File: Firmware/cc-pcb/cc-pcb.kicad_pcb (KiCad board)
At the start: 2 copper layers, 17 parts, among them CON1 BARREL_JACK, IC1 ATMEGA328P-A, P1 CONN_6, P2 CONN_6, P3 CONN_10, P4 CONN_6, P5 CONN_6, SW1 SRS

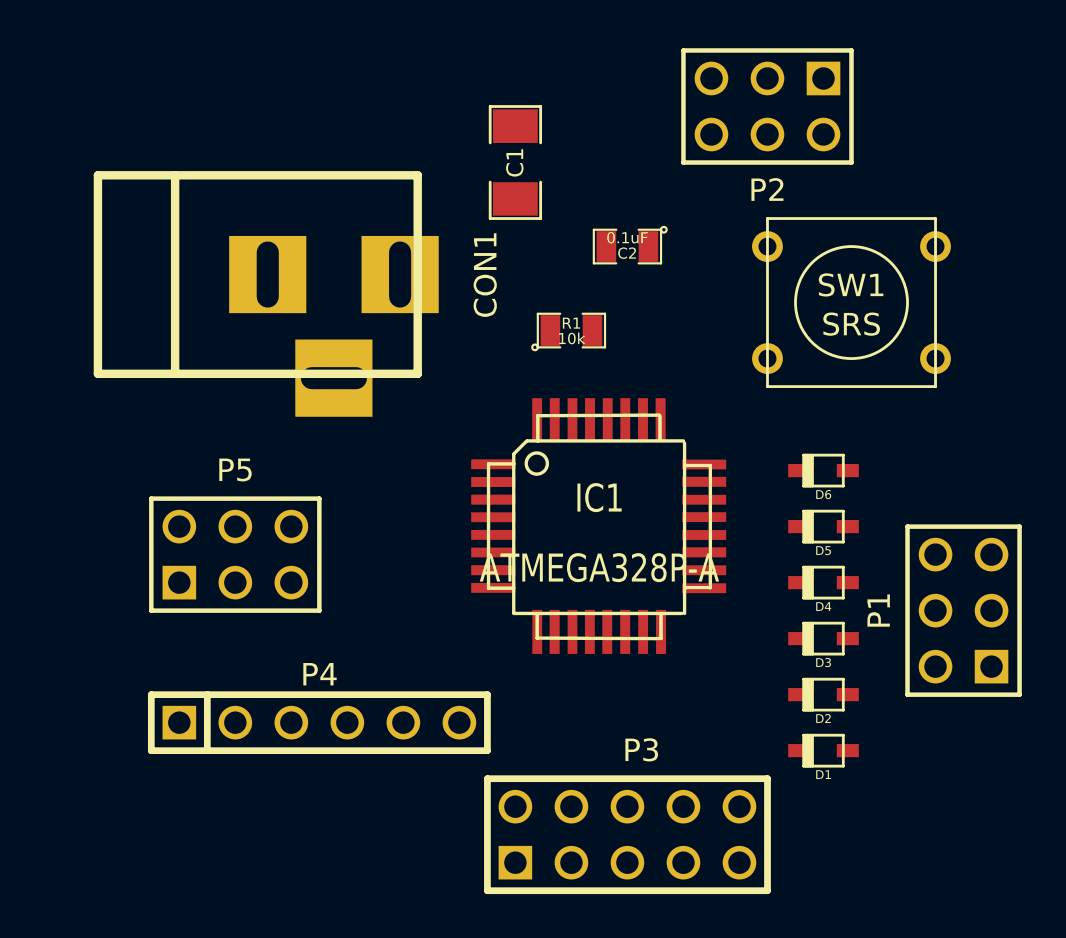
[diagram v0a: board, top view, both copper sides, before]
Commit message: Working on PCB, starting to make routes
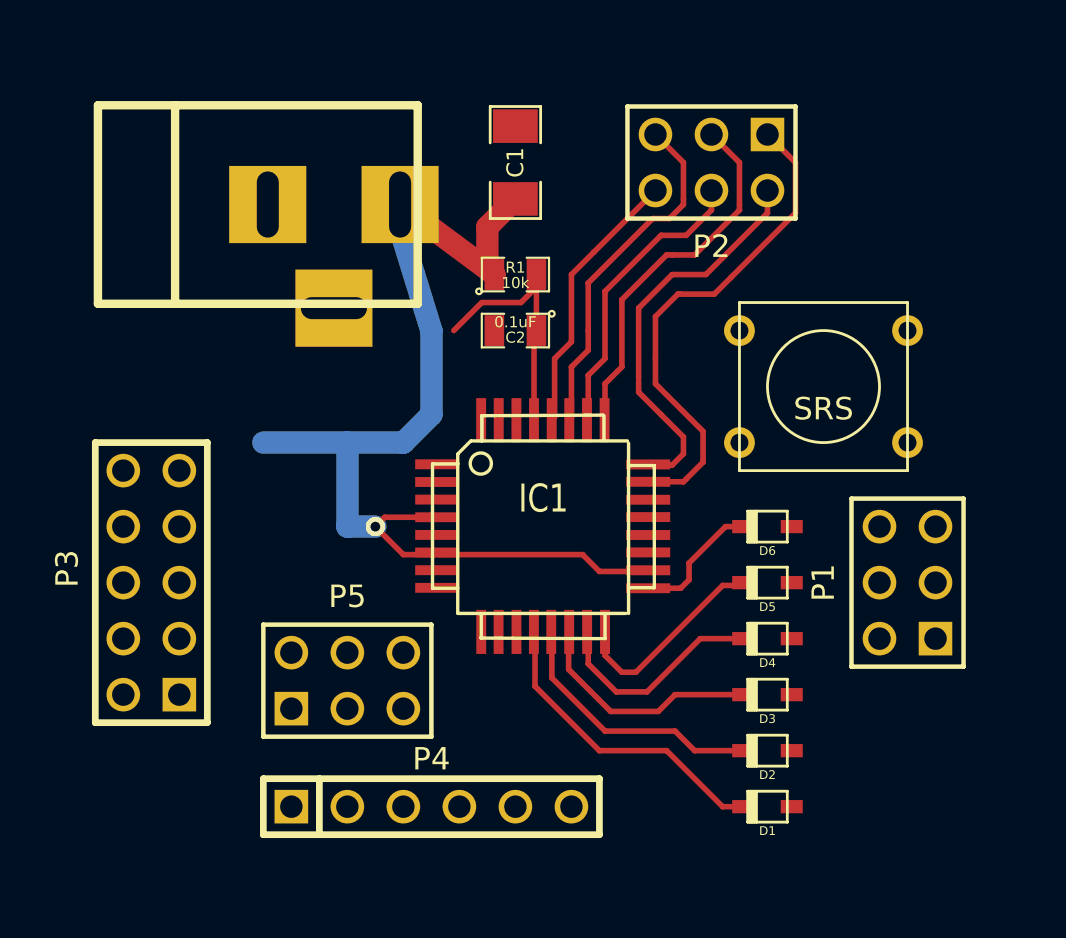
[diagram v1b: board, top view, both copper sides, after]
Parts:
- ?: renamed from CON1; value BARREL_JACK -> (none)
- IC1: value ATMEGA328P-A -> (none)
- P1, P2, P4, P5: value CONN_6 -> (none)
- P3: value CONN_10 -> (none)
- moved P3 24.4 mm to (153.7, 95.2), turned to 90 degrees
- moved P5 7.65 mm to (162.6, 99.7)
- moved P4 6.35 mm to (166.4, 105.4)
- moved C2 6.35 mm to (170.2, 83.8)
- moved ? 4.02 mm to (184.2, 86.4)
- moved P2 3.59 mm to (179.1, 76.2)
- moved D2 3.59 mm to (181.6, 102.9)
- moved D4 3.59 mm to (181.6, 97.8)
- moved D5 3.59 mm to (181.6, 95.2)
- moved D1 3.59 mm to (181.6, 105.4)
- moved D3 3.59 mm to (181.6, 100.3)
- moved D6 3.59 mm to (181.6, 92.7)
- moved R1 3.59 mm to (170.2, 81.3)
- moved ? 3.17 mm to (158.8, 78.1)
- moved P1 2.84 mm to (188.0, 95.2)
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- renumbered SW1 to ?
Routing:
- net VCC: track 0.00 -> 48.7 mm, vias 0 -> 1
- net N-000008: track 0.00 -> 22.7 mm
- net N-0000024: track 0.00 -> 17.8 mm
- net N-0000023: track 0.00 -> 16.8 mm
- net N-0000021: track 0.00 -> 16.1 mm
- net N-0000019: track 0.00 -> 14.3 mm
- net N-0000022: track 0.00 -> 13.4 mm
- net N-0000020: track 0.00 -> 12.4 mm
- net N-000009: track 0.00 -> 12.2 mm
- net N-0000029: track 0.00 -> 11.8 mm
- net N-0000018: track 0.00 -> 10.8 mm
- net N-0000017: track 0.00 -> 10.1 mm
- net N-0000016: track 0.00 -> 9.33 mm
- net N-0000015: track 0.00 -> 5.91 mm
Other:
- net class PWR added: clearance 0.508, trace_width 1.016, via_dia 0.889, via_drill 0.635

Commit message: Removed all traces from PCB
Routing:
- net VCC: track 48.7 -> 0.00 mm, vias 1 -> 0
- net N-000008: track 22.7 -> 0.00 mm
- net N-0000024: track 17.8 -> 0.00 mm
- net N-0000023: track 16.8 -> 0.00 mm
- net N-0000021: track 16.1 -> 0.00 mm
- net N-0000019: track 14.3 -> 0.14 mm
- net N-0000022: track 13.4 -> 0.00 mm
- net N-0000020: track 12.4 -> 0.00 mm
- net N-000009: track 12.2 -> 0.07 mm
- net N-0000029: track 11.8 -> 0.00 mm
- net N-0000018: track 10.8 -> 0.11 mm
- net N-0000017: track 10.1 -> 0.14 mm
- net N-0000016: track 9.33 -> 0.00 mm
- net N-0000015: track 5.91 -> 0.00 mm

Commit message: Working on PCB
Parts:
- moved P4 16.5 mm to (182.9, 105.4)
- moved P2 12.6 mm to (188.0, 85.1), turned to 90 degrees
- moved ? 10.9 mm to (177.8, 77.5)
- moved P5 6.75 mm to (167.6, 104.1)
- moved D2 6.48 mm to (180.3, 96.5)
- moved D4 6.48 mm to (180.3, 91.4)
- moved D1 6.48 mm to (180.3, 99.1)
- moved D3 6.48 mm to (180.3, 94.0)
- moved D5 6.48 mm to (180.3, 88.9)
- moved D6 6.48 mm to (180.3, 86.4)
- moved P3 5.24 mm to (158.8, 94.0)
- moved IC1 1.27 mm to (170.2, 92.7)
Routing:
- net VCC: track 0.00 -> 13.6 mm
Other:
- board outline added: 39.4 x 36.8 mm
- net class PWRIC added: clearance 0.254, trace_width 0.508, via_dia 0.889, via_drill 0.635
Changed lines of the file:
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@@
   (general
     (links 56)
-    (no_connects 56)
-    (area 148.7424 70.98792 192.8876 108.6866)
+    (no_connects 55)
+    (area 150.550879 70.98792 193.090001 109.270001)
     (thickness 1.6)
-    (drawings 0)
-    (tracks 11)
+    (drawings 4)
+    (tracks 14)
     (zones 0)
     (modules 17)
@@
     (add_net N-000008)
     (add_net N-000009)
-    (add_net VCC)
   )
   (net_class PWR ""
@@
     (uvia_drill 0.127)
   )
+  (net_class PWRIC ""
+    (clearance 0.254)
+    (trace_width 0.508)
+    (via_dia 0.889)
+    (via_drill 0.635)
+    (uvia_dia 0.508)
+    (uvia_drill 0.127)
+    (add_net VCC)
+  )
   (module TQFP32 (layer F.Cu)
-    (at 171.45 92.71)
+    (at 170.18 92.71)
     (fp_text reference IC1 (at 0 -1.27) (layer F.SilkS)
       (effects (font (size 1.27 1.016) (thickness 0.2032)))
@@
   )
   (module SW_PUSH_SMALL (layer F.Cu)
-    (at 184.15 86.36)
+    (at 177.8 77.47)
     (fp_text reference "" (at 0 -0.762) (layer F.SilkS)
       (effects (font (size 1.016 1.016) (thickness 0.2032)))
@@
   )
   (module sod323 (layer F.Cu)
-    (at 181.61 105.41 180)
+    (at 180.34 99.06 180)
     (descr SOD323)
     (fp_text reference D1 (at 0 -1.09982 180) (layer F.SilkS)
@@
   )
   (module sod323 (layer F.Cu)
-    (at 181.61 102.87 180)
+    (at 180.34 96.52 180)
     (descr SOD323)
     (fp_text reference D2 (at 0 -1.09982 180) (layer F.SilkS)
@@
   )
   (module sod323 (layer F.Cu)
-    (at 181.61 100.33 180)
+    (at 180.34 93.98 180)
     (descr SOD323)
     (fp_text reference D3 (at 0 -1.09982 180) (layer F.SilkS)
@@
   )
   (module sod323 (layer F.Cu)
-    (at 181.61 97.79 180)
+    (at 180.34 91.44 180)
     (descr SOD323)
     (fp_text reference D4 (at 0 -1.09982 180) (layer F.SilkS)
@@
   )
   (module sod323 (layer F.Cu)
-    (at 181.61 95.25 180)
+    (at 180.34 88.9 180)
     (descr SOD323)
     (fp_text reference D5 (at 0 -1.09982 180) (layer F.SilkS)
@@
   )
   (module sod323 (layer F.Cu)
-    (at 181.61 92.71 180)
+    (at 180.34 86.36 180)
     (descr SOD323)
     (fp_text reference D6 (at 0 -1.09982 180) (layer F.SilkS)
@@
   )
   (module PIN_ARRAY_5x2 (layer F.Cu)
-    (at 153.67 95.25 90)
+    (at 158.75 93.98 90)
     (descr "Double rangee de contacts 2 x 5 pins")
     (tags CONN)
@@
   )
   (module pin_array_3x2 (layer F.Cu)
-    (at 162.56 99.695)
+    (at 167.64 104.14)
     (descr "Double rangee de contacts 2 x 4 pins")
     (tags CONN)
@@
   )
   (module PIN_ARRAY-6X1 (layer F.Cu)
-    (at 166.37 105.41)
+    (at 182.88 105.41)
     (descr "Connecteur 6 pins")
     (tags "CONN DEV")
@@
   )
   (module pin_array_3x2 (layer F.Cu)
-    (at 179.07 76.2 180)
+    (at 187.96 85.09 90)
     (descr "Double rangee de contacts 2 x 4 pins")
     (tags CONN)
-    (fp_text reference P2 (at 0 -3.81 180) (layer F.SilkS)
-      (effects (font (size 1.016 1.016) (thickness 0.2032)))
-    )
-    (fp_text value "" (at 0 3.81 180) (layer F.SilkS) hide
+    (fp_text reference P2 (at 0 -3.81 90) (layer F.SilkS)
+      (effects (font (size 1.016 1.016) (thickness 0.2032)))
+    )
+    (fp_text value "" (at 0 3.81 90) (layer F.SilkS) hide
       (effects (font (size 1.016 1.016) (thickness 0.2032)))
     )
@@
     (fp_line (start 3.81 -2.54) (end 3.81 2.54) (layer F.SilkS) (width 0.2032))
     (fp_line (start -3.81 2.54) (end -3.81 -2.54) (layer F.SilkS) (width 0.2032))
-    (pad 1 thru_hole rect (at -2.54 1.27 180) (size 1.524 1.524) (drill 1.016)
+    (pad 1 thru_hole rect (at -2.54 1.27 90) (size 1.524 1.524) (drill 1.016)
       (layers *.Cu *.Mask F.SilkS)
       (net 29 N-000008)
     )
-    (pad 2 thru_hole circle (at -2.54 -1.27 180) (size 1.524 1.524) (drill 1.016)
+    (pad 2 thru_hole circle (at -2.54 -1.27 90) (size 1.524 1.524) (drill 1.016)
       (layers *.Cu *.Mask F.SilkS)
       (net 18 N-0000024)
     )
-    (pad 3 thru_hole circle (at 0 1.27 180) (size 1.524 1.524) (drill 1.016)
+    (pad 3 thru_hole circle (at 0 1.27 90) (size 1.524 1.524) (drill 1.016)
       (layers *.Cu *.Mask F.SilkS)
       (net 17 N-0000023)
     )
-    (pad 4 thru_hole circle (at 0 -1.27 180) (size 1.524 1.524) (drill 1.016)
+    (pad 4 thru_hole circle (at 0 -1.27 90) (size 1.524 1.524) (drill 1.016)
       (layers *.Cu *.Mask F.SilkS)
       (net 16 N-0000022)
     )
-    (pad 5 thru_hole circle (at 2.54 1.27 180) (size 1.524 1.524) (drill 1.016)
+    (pad 5 thru_hole circle (at 2.54 1.27 90) (size 1.524 1.524) (drill 1.016)
       (layers *.Cu *.Mask F.SilkS)
       (net 15 N-0000021)
     )
-    (pad 6 thru_hole circle (at 2.54 -1.27 180) (size 1.524 1.524) (drill 1.016)
+    (pad 6 thru_hole circle (at 2.54 -1.27 90) (size 1.524 1.524) (drill 1.016)
       (layers *.Cu *.Mask F.SilkS)
       (net 14 N-0000020)
@@
     )
   )
-  (segment (start 170.307 97.5614) (end 170.2308 97.4852) (width 0.254) (layer F.Cu) (net 2))
-  (segment (start 170.307 97.5614) (end 170.2308 97.4852) (width 0.254) (layer F.Cu) (net 2) (status 30))
-  (segment (start 173.482 97.536) (end 173.4312 97.4852) (width 0.254) (layer F.Cu) (net 10))
-  (segment (start 173.4312 97.4852) (end 173.482 97.536) (width 0.254) (layer F.Cu) (net 10) (status 30))
-  (segment (start 172.593 97.5106) (end 172.6184 97.4852) (width 0.254) (layer F.Cu) (net 11))
-  (segment (start 172.593 97.5106) (end 172.6184 97.4852) (width 0.254) (layer F.Cu) (net 11))
-  (segment (start 172.6184 97.4852) (end 172.593 97.5106) (width 0.254) (layer F.Cu) (net 11) (status 30))
-  (segment (start 171.069 97.536) (end 171.0182 97.4852) (width 0.254) (layer F.Cu) (net 12))
-  (segment (start 171.0182 97.4852) (end 171.069 97.536) (width 0.254) (layer F.Cu) (net 12) (status 30))
-  (segment (start 171.831 97.5106) (end 171.8056 97.4852) (width 0.254) (layer F.Cu) (net 30))
-  (segment (start 171.8056 97.4852) (end 171.831 97.5106) (width 0.254) (layer F.Cu) (net 30) (status 30))
+  (gr_line (start 153.67 109.22) (end 153.67 72.39) (angle 90) (layer Edge.Cuts) (width 0.1))
+  (gr_line (start 193.04 109.22) (end 153.67 109.22) (angle 90) (layer Edge.Cuts) (width 0.1))
+  (gr_line (start 193.04 72.39) (end 193.04 109.22) (angle 90) (layer Edge.Cuts) (width 0.1))
+  (gr_line (start 153.67 72.39) (end 193.04 72.39) (angle 90) (layer Edge.Cuts) (width 0.1))
+  (segment (start 169.037 97.5614) (end 168.9608 97.4852) (width 0.254) (layer F.Cu) (net 2) (status 30))
+  (segment (start 169.037 97.5614) (end 168.9608 97.4852) (width 0.254) (layer F.Cu) (net 2) (status 30))
+  (segment (start 172.212 97.536) (end 172.1612 97.4852) (width 0.254) (layer F.Cu) (net 10) (status 30))
+  (segment (start 172.1612 97.4852) (end 172.212 97.536) (width 0.254) (layer F.Cu) (net 10) (status 30))
+  (segment (start 171.323 97.5106) (end 171.3484 97.4852) (width 0.254) (layer F.Cu) (net 11) (status 30))
+  (segment (start 171.323 97.5106) (end 171.3484 97.4852) (width 0.254) (layer F.Cu) (net 11) (status 30))
+  (segment (start 171.3484 97.4852) (end 171.323 97.5106) (width 0.254) (layer F.Cu) (net 11) (status 30))
+  (segment (start 169.799 97.536) (end 169.7482 97.4852) (width 0.254) (layer F.Cu) (net 12) (status 30))
+  (segment (start 169.7482 97.4852) (end 169.799 97.536) (width 0.254) (layer F.Cu) (net 12) (status 30))
+  (segment (start 170.561 97.5106) (end 170.5356 97.4852) (width 0.254) (layer F.Cu) (net 30) (status 30))
+  (segment (start 170.5356 97.4852) (end 170.561 97.5106) (width 0.254) (layer F.Cu) (net 30) (status 30))
+  (segment (start 161.29 88.9) (end 160.02 88.9) (width 1.016) (layer B.Cu) (net 31))
+  (segment (start 164.95014 85.23986) (end 161.29 88.9) (width 1.016) (layer B.Cu) (net 31))
+  (segment (start 164.95014 78.105) (end 164.95014 85.23986) (width 1.016) (layer B.Cu) (net 31))
 )

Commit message: autorouter
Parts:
- moved D2 1.78 mm to (180.3, 98.3)
- moved D4 1.78 mm to (180.3, 93.2)
- moved D6 1.78 mm to (180.3, 88.1)
- moved D1 1.78 mm to (180.3, 100.8)
- moved D3 1.78 mm to (180.3, 95.8)
- moved D5 1.78 mm to (180.3, 90.7)
- turned P3 to 270 degrees
- gave numbers to parts that had none: 2
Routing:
- net GND: track 0.00 -> 111.3 mm, vias 0 -> 1
- net VCC: track 13.6 -> 85.5 mm, vias 0 -> 1
- net N-0000015: track 0.00 -> 56.4 mm
- net N-0000016: track 0.00 -> 56.3 mm, vias 0 -> 1
- net N-0000028: track 0.00 -> 53.5 mm
- net N-0000030: track 0.00 -> 51.6 mm
- net N-000007: track 0.00 -> 49.7 mm
- net N-0000029: track 0.00 -> 49.6 mm, vias 0 -> 1
- net N-0000032: track 0.00 -> 33.1 mm, vias 0 -> 1
- net N-0000017: track 0.14 -> 32.6 mm
- net N-0000021: track 0.00 -> 20.9 mm
- net N-0000020: track 0.00 -> 19.2 mm
- net N-0000023: track 0.00 -> 18.5 mm
- net N-000008: track 0.00 -> 17.8 mm
- net N-0000022: track 0.00 -> 16.5 mm
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
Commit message: added mounting holes
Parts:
- added 1PIN: P***, 1pin, F.Cu at (190.5, 106.7)
- added 1PIN: P***, 1pin, F.Cu at (190.5, 74.9)
- added 1PIN: P***, 1pin, F.Cu at (156.2, 106.7)
- moved P4 15.2 mm to (167.6, 105.4)
- moved P5 15.2 mm to (182.9, 104.1)
- moved D1 5.11 mm to (175.3, 100.3)
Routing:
- net N-0000015: track 56.4 -> 0.00 mm
- net N-0000016: track 56.3 -> 0.00 mm, vias 1 -> 0
- net N-0000028: track 53.5 -> 0.00 mm
- net N-0000030: track 51.6 -> 0.00 mm
- net N-0000029: track 49.6 -> 2.54 mm, vias 1 -> 0
- net N-000007: track 49.7 -> 9.88 mm
- net GND: track 111.3 -> 77.0 mm
- net N-0000017: track 32.6 -> 0.00 mm
- net VCC: track 85.5 -> 57.5 mm
- net N-000008: track 17.8 -> 0.00 mm
- net N-000006: track 12.4 -> 0.00 mm
- net N-0000019: track 11.7 -> 0.00 mm
- net N-000009: track 11.6 -> 0.00 mm
- net N-0000018: track 11.2 -> 0.04 mm
- net N-0000010: track 9.98 -> 0.00 mm
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
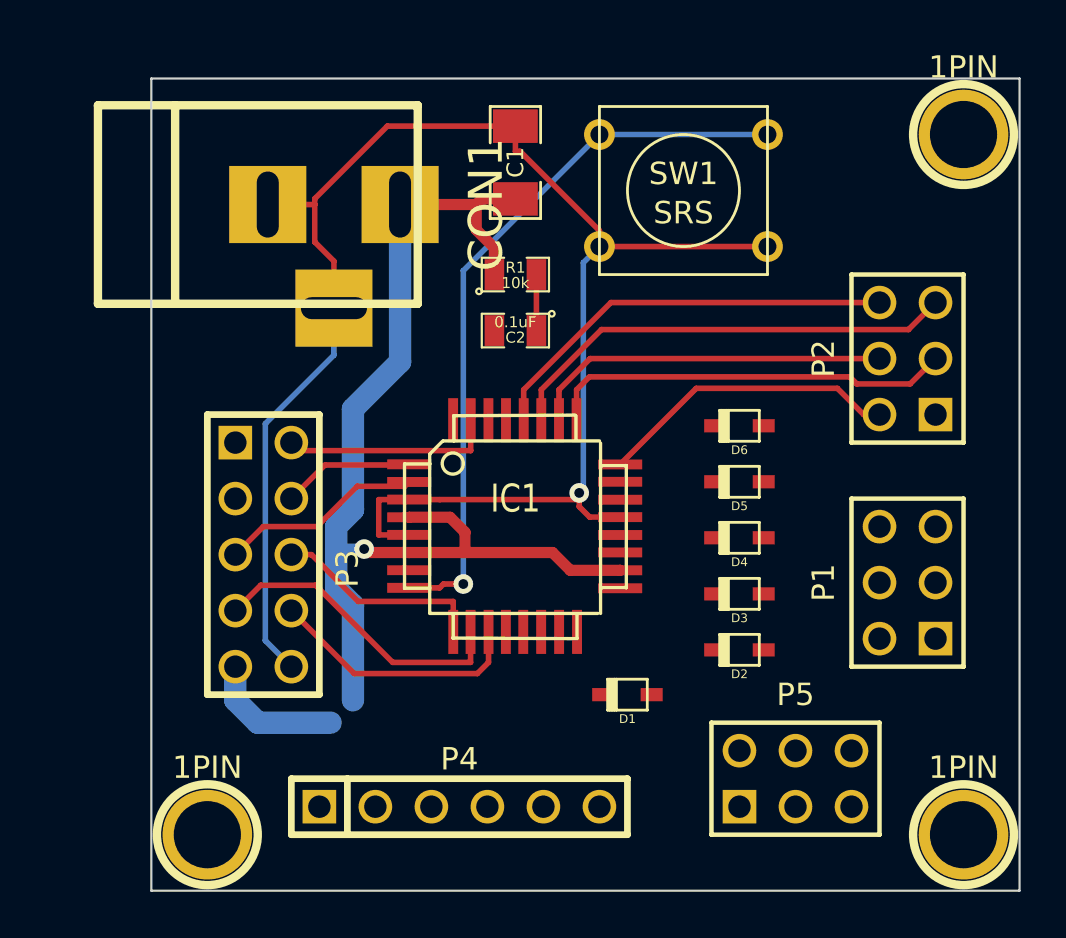
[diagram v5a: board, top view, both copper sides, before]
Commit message: adjusting colors
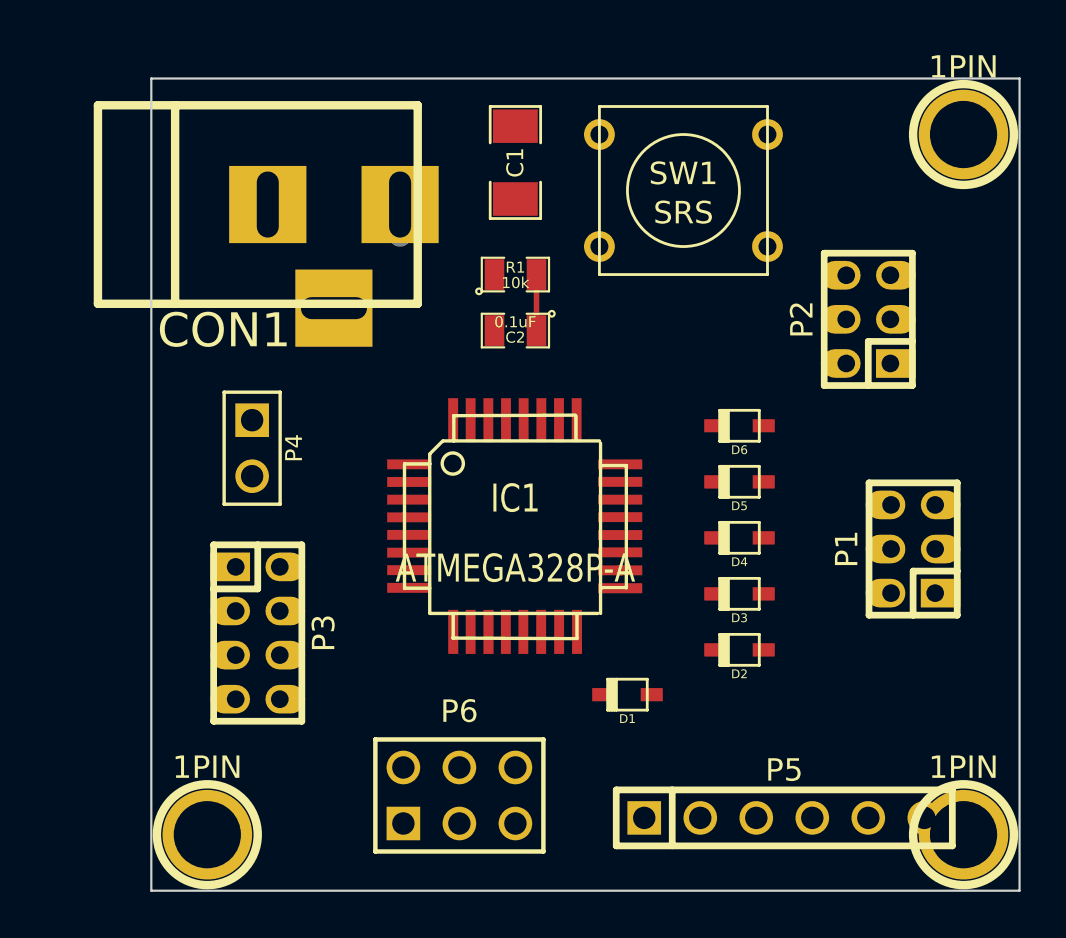
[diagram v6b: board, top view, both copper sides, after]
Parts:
- added P6: CONN_6, pin_array_3x2, F.Cu at (167.6, 104.9)
- CON1: value (none) -> BARREL_JACK
- IC1: value (none) -> ATMEGA328P-A
- P1, P2: value (none) -> CONN_6; footprint pin_array_3x2 -> pin_socket_2mm_3x2
- P3: value (none) -> CONN_8; footprint PIN_ARRAY_5x2 -> pin_socket_2mm_4x2
- P4: value (none) -> CONN_2; footprint PIN_ARRAY-6X1 -> PIN_ARRAY_2X1
- P5: value (none) -> CONN_6; footprint pin_array_3x2 -> PIN_ARRAY-6X1
- moved P4 18.8 mm to (158.2, 89.2), turned to 270 degrees
- moved P3 3.57 mm to (158.5, 97.5)
- moved P2 2.51 mm to (186.2, 83.3)
- moved P5 1.85 mm to (182.4, 105.9)
- moved P1 1.55 mm to (188.2, 93.7)
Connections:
- C2 pad 1: N-0000029 -> N-000003
- C2 pad 2: N-0000030 -> N-000004
- D4 pad 2: N-0000017 (its old number) -> N-000008
- D5 pad 2: N-0000016 (its old number) -> N-000007
- D6 pad 2: N-0000015 (its old number) -> N-000006
- IC1 pad 15: N-0000017 (its old number) -> N-000008
- IC1 pad 16: N-0000016 (its old number) -> N-000007
- IC1 pad 17: N-0000015 (its old number) -> N-000006
- IC1 pad 29: N-0000029 -> N-000003
- IC1 pad 30: N-0000028 -> N-0000024
- IC1 pad 31: N-000007 -> N-000002
- P3 pad 1: N-0000028 -> N-0000024
- P3 pad 2: N-000007 -> N-000002
- P4 pad 1: N-0000030 -> VCC
- P4 pad 2: N-000007 -> GND
- P5 pad 1: N-0000016 (its old number) -> N-000004
- P5 pad 2: VCC -> N-000002
- P5 pad 3: N-0000015 (its old number) -> N-0000024
- P5 pad 4: N-0000017 (its old number) -> VCC
- P5 pad 5: N-0000029 -> GND
- R1 pad 2: N-0000029 -> N-000003
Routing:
- net GND: track 77.0 -> 0.00 mm, vias 1 -> 0
- net VCC: track 57.5 -> 2.82 mm, vias 1 -> 0
- net N-0000025: track 33.1 -> 0.00 mm, vias 1 -> 0
- net N-0000017: track 20.9 -> 0.00 mm
- net N-000005: track 19.2 -> 0.00 mm
- net N-0000019: track 18.5 -> 0.00 mm
- net N-0000018: track 16.5 -> 0.00 mm
- net N-0000013: track 14.0 -> 0.00 mm
- net N-0000020: track 13.7 -> 0.00 mm
- net N-0000012: track 11.7 -> 0.00 mm
- net N-000007: track 9.88 -> 0.00 mm
- net N-0000014: track 9.60 -> 0.00 mm
- net N-0000015: track 9.26 -> 0.01 mm
- net N-0000016: track 5.99 -> 0.00 mm
- net N-000003: track 0.00 -> 2.54 mm
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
